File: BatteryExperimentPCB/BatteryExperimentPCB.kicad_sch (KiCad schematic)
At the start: 20 parts, among them J1 Screw_Terminal_01x02, J2 Conn_01x10_Pin, J3 Conn_01x10_Pin, U1 BQ25628RYKR, U2 ATtiny3226-M

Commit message: wiring lots of stuff up
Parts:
- removed BT1: Battery_Cell, symbol Device:Battery_Cell
- removed J1: Screw_Terminal_01x02, symbol Connector:Screw_Terminal_01x02
- removed J2, J3: Conn_01x10_Pin, Connector_PinHeader_2.54mm:PinHeader_1x10_P2.54mm_Vertical, symbol Connector:Conn_01x10_Pin
- removed R1: R_Small, symbol Device:R_Small
- removed TP1: TestPoint, symbol Connector:TestPoint
- added C4, C5: C_Small, symbol Device:C_Small
- added J1: USB_C_Receptacle_USB2.0_14P, Connector_USB:USB_C_Receptacle_G-Switch_GT-USB-7025, symbol Connector:USB_C_Receptacle_USB2.0_14P
- added J2, J4: Conn_01x11_Pin, symbol Connector:Conn_01x11_Pin
- added Q1: DMG1012T, Package_TO_SOT_SMD:SOT-523, symbol Transistor_FET:DMG1012T
- added R1: 2.2k, Resistor_SMD:R_0201_0603Metric, symbol Device:R
- added R2, R3: 68, Resistor_SMD:R_0201_0603Metric, symbol Device:R
- added R7: 620k, symbol Device:R
- added R8: 240k, symbol Device:R
- added SW1: SW_Push, symbol Switch:SW_Push
- added U1: USBLC6-2P6, Package_TO_SOT_SMD:SOT-666, symbol Power_Protection:USBLC6-2P6
- renumbered C2 to C1, C1 to C2, D2 to D1, D1 to D2, R3 to R10, R4 to R11, R5 to R4, R6 to R5, R7 to R6, R2 to R9, U1 to U3
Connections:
- net STATUS/FAULT host Interrupt is gone; now on net StatusInterrupt: R11.1, U3.11 (INT)
- net BulbLED: now also J2.6 (Pin_6)
- net Button: now also J2.5 (Pin_5), SW1.1
- net BypassMCU: now also C5.2
- net ChargeEnable: now also U2.14 (PB0)
- net D+: now also J2.3 (Pin_3), R2.1
- net D-: now also J2.4 (Pin_4), R3.1
- net GND: now also C4.1, C5.1, J1.A1 (GND), J1.A12 (GND), J1.B1 (GND), J1.B12 (GND), J4.10 (Pin_10), J4.7 (Pin_7), J4.8 (Pin_8), J4.9 (Pin_9), R8.2, SW1.2, U1.2 (GND)
- net SCL: now also U2.13 (PB1), J2.9 (Pin_9); no longer U2.14 (PB0)
- net SDA: now also U2.12 (PB2), J2.10 (Pin_10); no longer U2.13 (PB1)
- net VBUS: now reaches U3.18 (VBUS)
- net VBUS: now also J1.A4 (VBUS), J1.A9 (VBUS), J1.B4 (VBUS), J1.B9 (VBUS), J4.11 (Pin_11), R1.2, U1.5 (VBUS)
- net QON: now reaches U3.7 (QON)
- net QON: now also J4.4 (Pin_4)
- net CaseBlue: now reaches R6.2, U2.17 (PC2)
- net CaseRed: now reaches R4.2, U2.15 (PC0)
- net PB4: now reaches U2.10 (PB4)
- net PB4: now also J4.1 (Pin_1)
- net StatusInterrupt: now reaches U2.11 (PB3)
- net StatusInterrupt: now also J2.11 (Pin_11)
- net CaseGreen: now reaches R5.2, U2.16 (PC1)
- net PC3: now reaches U2.18 (PC3)
- net PC3: now also J4.3 (Pin_3)
- net VoltageMonitor: now reaches U2.7 (PA6)
- net VoltageMonitor: now also R7.2, R8.1
- net VoltageMonitorEnable: now reaches U2.8 (PA7)
- net VoltageMonitorEnable: now also Q1.1 (G)
- net PB5: now reaches U2.9 (PB5)
- net PB5: now also J4.2 (Pin_2)
- net Battery renamed Battery+
- net Battery+: now also C4.2, J4.6 (Pin_6), Q1.2 (S)
- net Program renamed Reset
- net Reset: now also J2.1 (Pin_1)
- net VoltageMonitorADC renamed PA1
- net PA1: now also J2.2 (Pin_2)
- new net: Q1.3 (D), R7.1
- new net: R3.2, U1.4 (I/O2)
- new net: R2.2, U1.3 (I/O2)
- new net DBUS+: J1.A6 (D+), J1.B6 (D+), U1.1 (I/O1)
- new net DBUS-: J1.A7 (D-), J1.B7 (D-), R1.1, U1.6 (I/O1)
- new net ILIM: J4.5 (Pin_5)
- no-connect marks 5 -> 8
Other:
- note added: "Battery Monitor"
- note added: "Charging"
- note added: "MCU"
- note added: "Peripherals"
- note added: "SET LOW SPEED USB"
- note added: "TODO: setup ILIM pin or leave floating and disable with EN_EXTILIM register, usb should already have max of 100 milliamps"
- note added: "USB / ESD"
- note added: "VoltageDivider to bring 5V down to 1V. (battery will probably max out at 4.5V) This will allow Attiny internal 1.024V voltage reference to be used to calculate battery voltage. Enabled via mosfet to keep voltage divider from draining battery."
- note removed: "Charge enable pull down resistor"
- note removed: "TODO: setup ILIM pin or disable with EN_EXTILIM register, usb should have max of 100 milliamps"
- moved on the sheet: C1, C2, C3, D1, D2, L1, R10, R11, R4, R5, R6, R9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

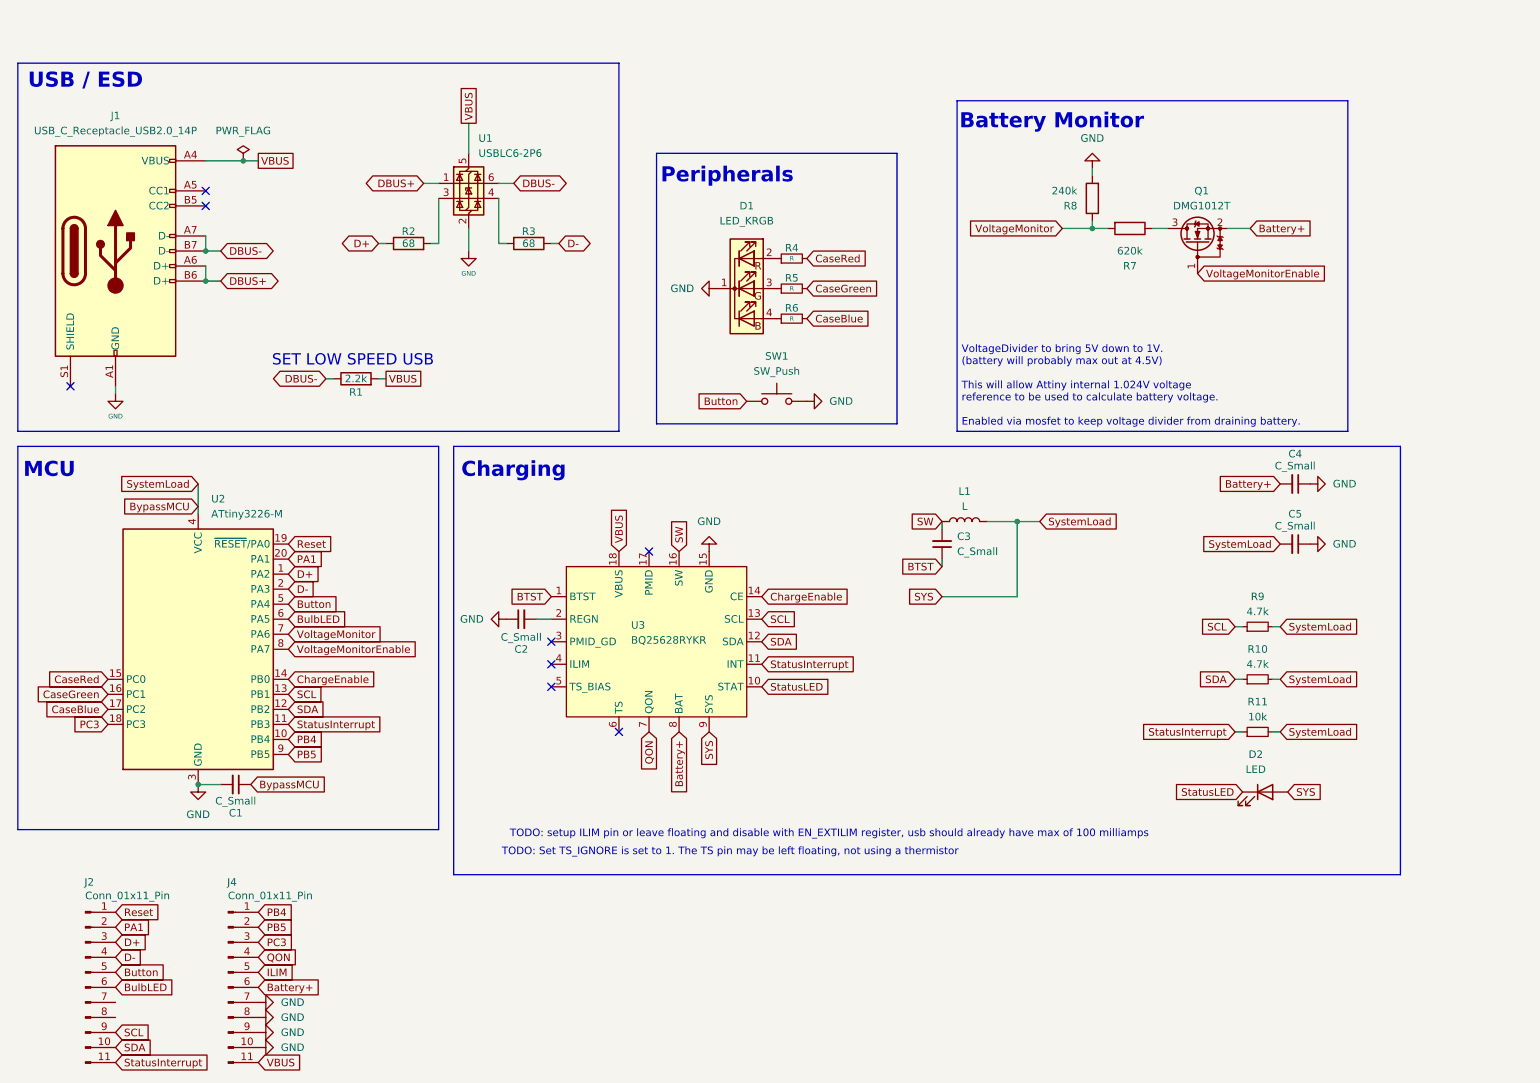
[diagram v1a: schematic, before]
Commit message: added mostfet to battery monitor voltage divider, cleanup
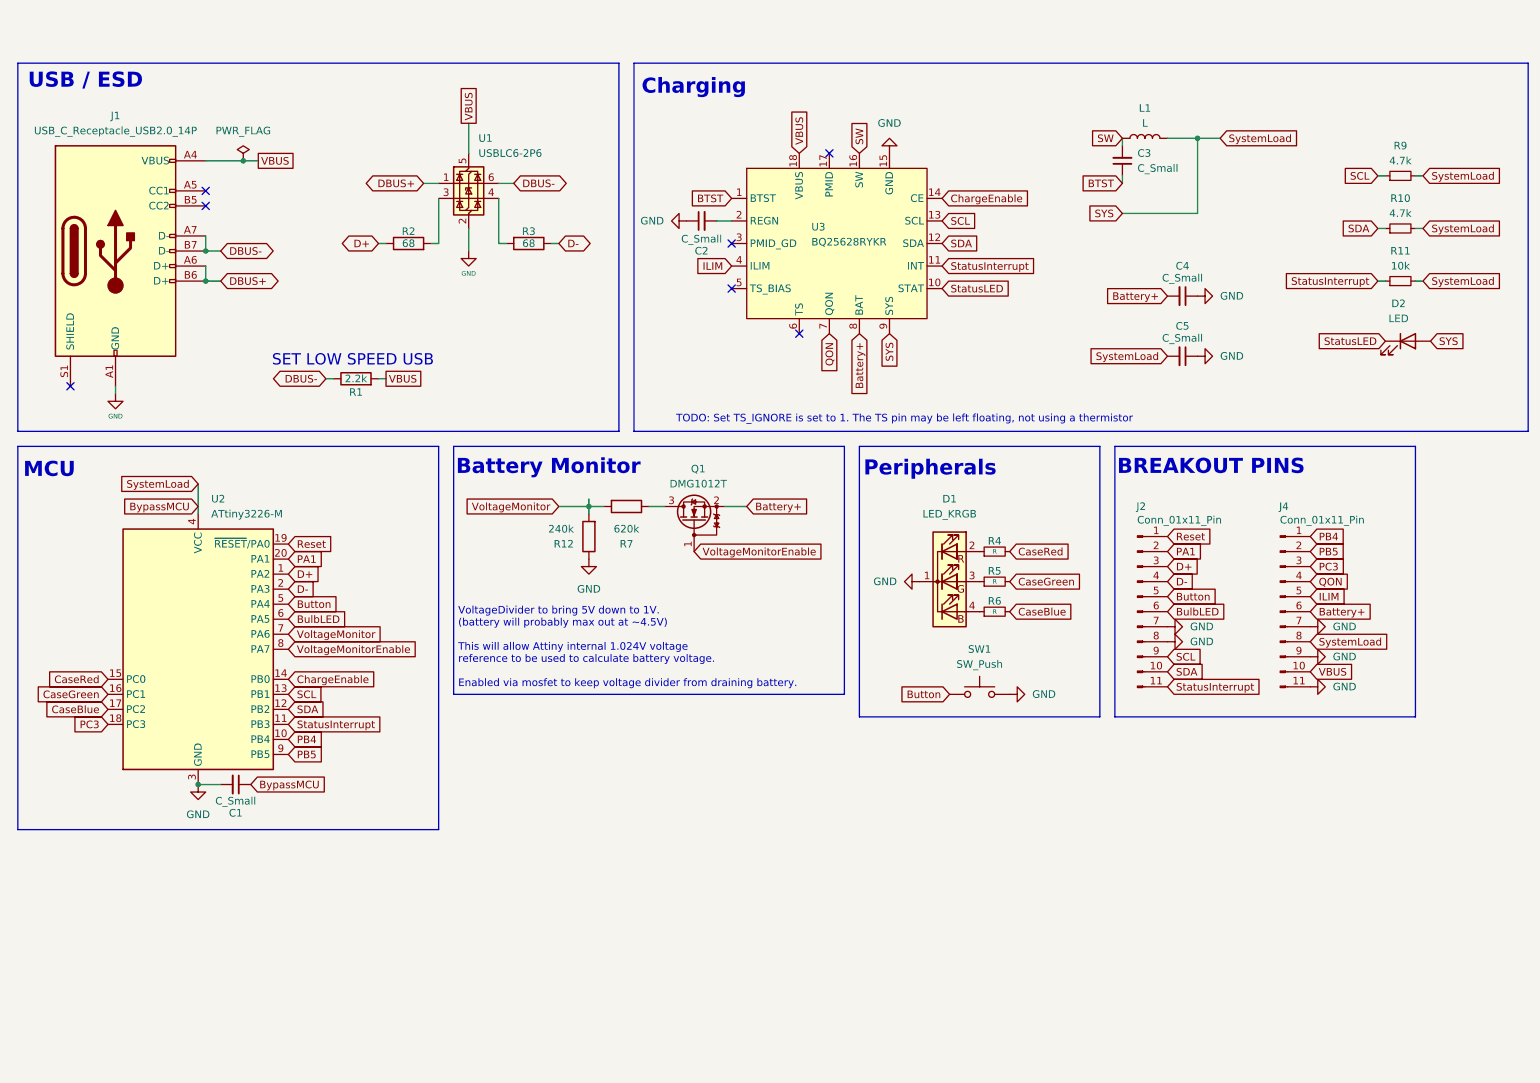
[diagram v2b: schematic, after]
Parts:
- removed R8: 240k, symbol Device:R
- added R12: 240k, symbol Device:R
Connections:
- net BypassMCU: now also J4.8 (Pin_8)
- net GND: now also J2.7 (Pin_7), J2.8 (Pin_8), J4.11 (Pin_11), R12.1; no longer J4.10 (Pin_10), J4.8 (Pin_8)
- net ILIM: now also U3.4 (ILIM)
- net VBUS: now also J4.10 (Pin_10); no longer J4.11 (Pin_11)
- net VoltageMonitor: now also R12.2
- no-connect marks 8 -> 7
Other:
- note added: "BREAKOUT PINS"
- note added: "VoltageDivider to bring 5V down to 1V. (battery will probably max out at ~4.5V) This will allow Attiny internal 1.024V voltage reference to be used to calculate battery voltage. Enabled via mosfet to keep voltage divider from draining battery."
- note removed: "TODO: setup ILIM pin or leave floating and disable with EN_EXTILIM register, usb should already have max of 100 milliamps"
- note removed: "VoltageDivider to bring 5V down to 1V. (battery will probably max out at 4.5V) This will allow Attiny internal 1.024V voltage reference to be used to calculate battery voltage. Enabled via mosfet to keep voltage divider from draining battery."
- moved on the sheet: C2, C3, C4, C5, D1, D2, J2, J4, L1, Q1, R10, R11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

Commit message: add resistors to usb cc pins, fix electrical rules checker errors
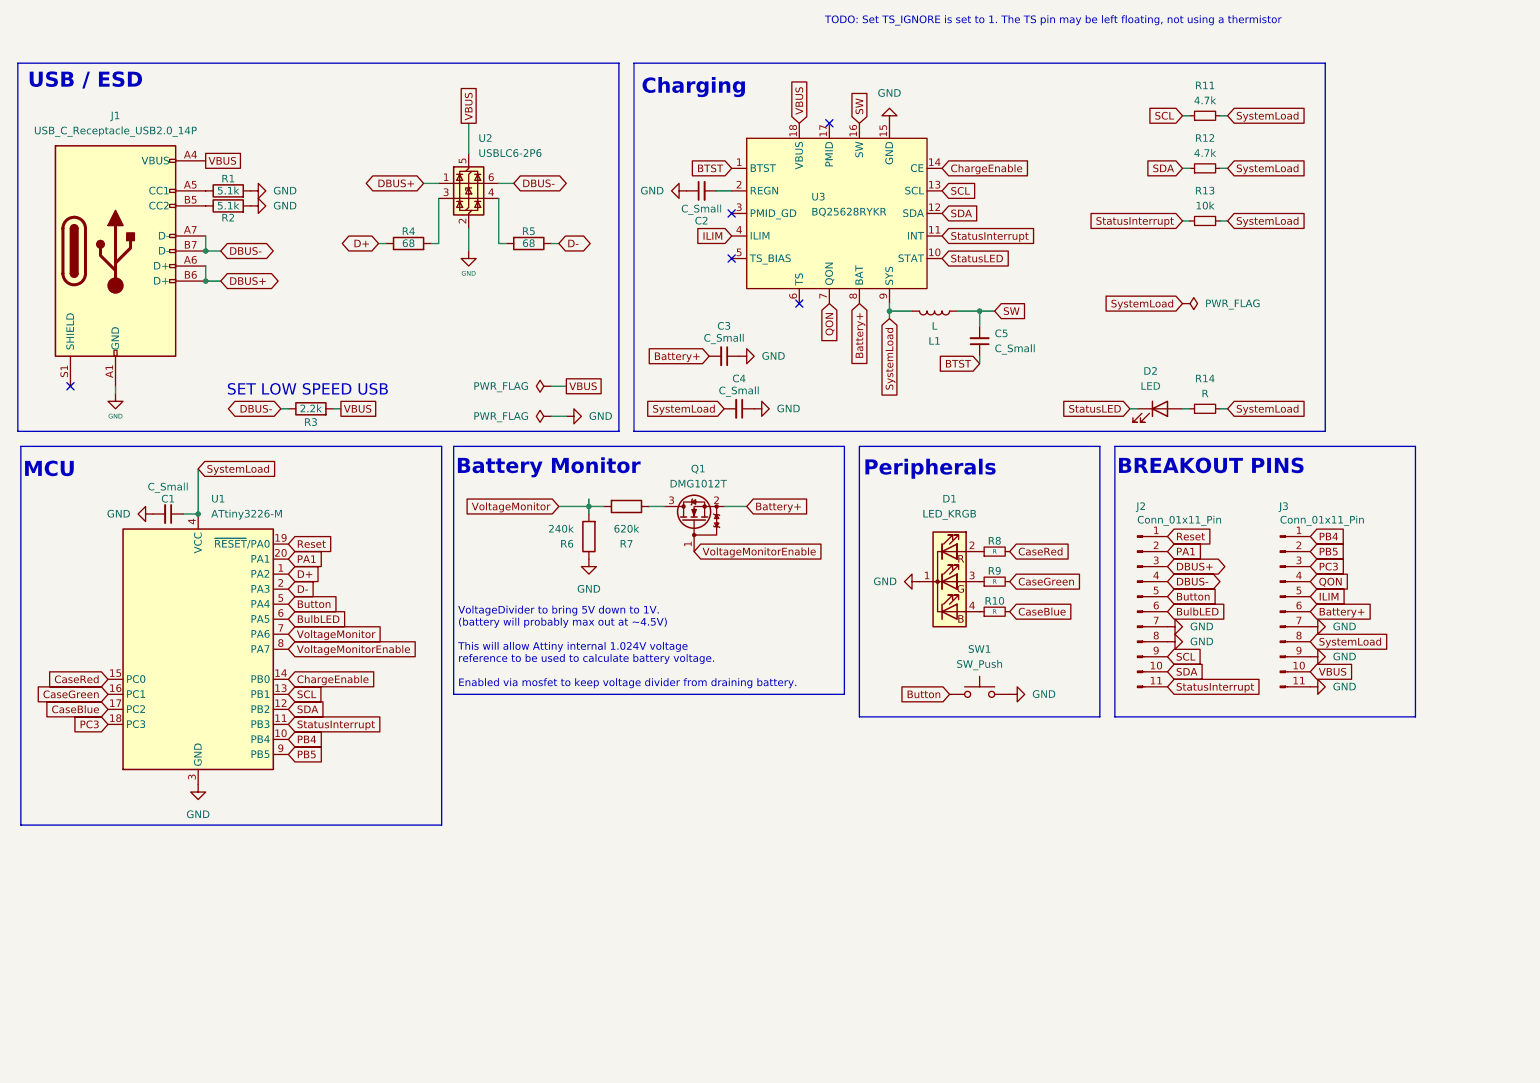
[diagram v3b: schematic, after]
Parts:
- removed C3: C_Small, symbol Device:C_Small
- added C5: C_Small, symbol Device:C_Small
- added R1, R2: 5.1k, Resistor_SMD:R_0201_0603Metric, symbol Device:R
- added R14: R, symbol Device:R_Small
- renumbered C4 to C3, C5 to C4, J4 to J3, R6 to R10, R9 to R11, R10 to R12, R11 to R13, R1 to R3, R2 to R4, R3 to R5, R12 to R6, R4 to R8, R5 to R9, U2 to U1, U1 to U2
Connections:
- net BTST: now also C5.1
- net D+: no longer J2.3 (Pin_3)
- net D-: no longer J2.4 (Pin_4)
- net DBUS+: now also J2.3 (Pin_3)
- net DBUS-: now also J2.4 (Pin_4)
- net GND: now also R1.2, R2.2
- net SW: now also C5.2
- net at J1.A5 (CC1): now also R1.1
- net at J1.B5 (CC2): now also R2.1
- net BypassMCU renamed SystemLoad
- net SystemLoad: now also R14.2; no longer D2.2 (A)
- new net: D2.2 (A), R14.1
- no-connect marks 7 -> 5
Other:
- moved on the sheet: C2, C3, C4, D2, R11, R12, R13, R3, U3
